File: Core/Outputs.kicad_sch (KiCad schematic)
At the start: 65 parts, among them J3 Conn_01x10_Female, J7 Conn_01x10_Female, Q14 2N7002, U10 TL072, U11 TL072, U12 TL072, U15 MAX5134, U2 TMUX1309, U4 TL072, U5 TL072, U6 TL072, U7 TL072, U8 TMUX1309, U9 TL072

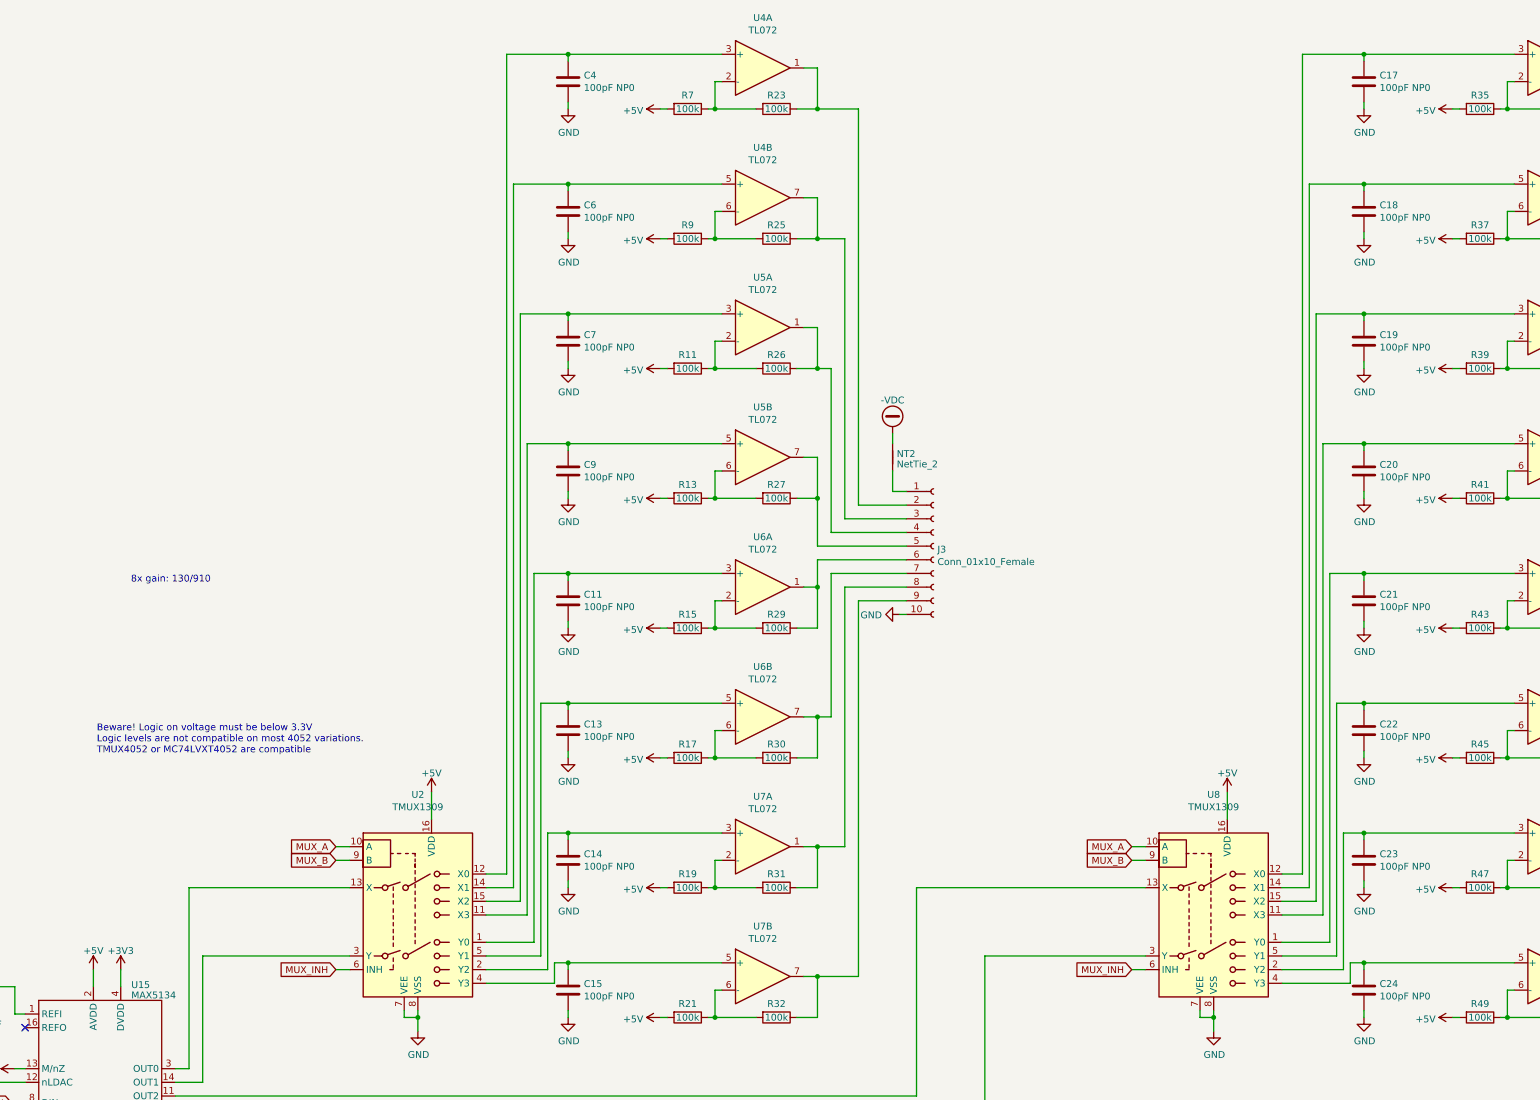
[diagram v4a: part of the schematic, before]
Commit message: Increase SnH capacitance
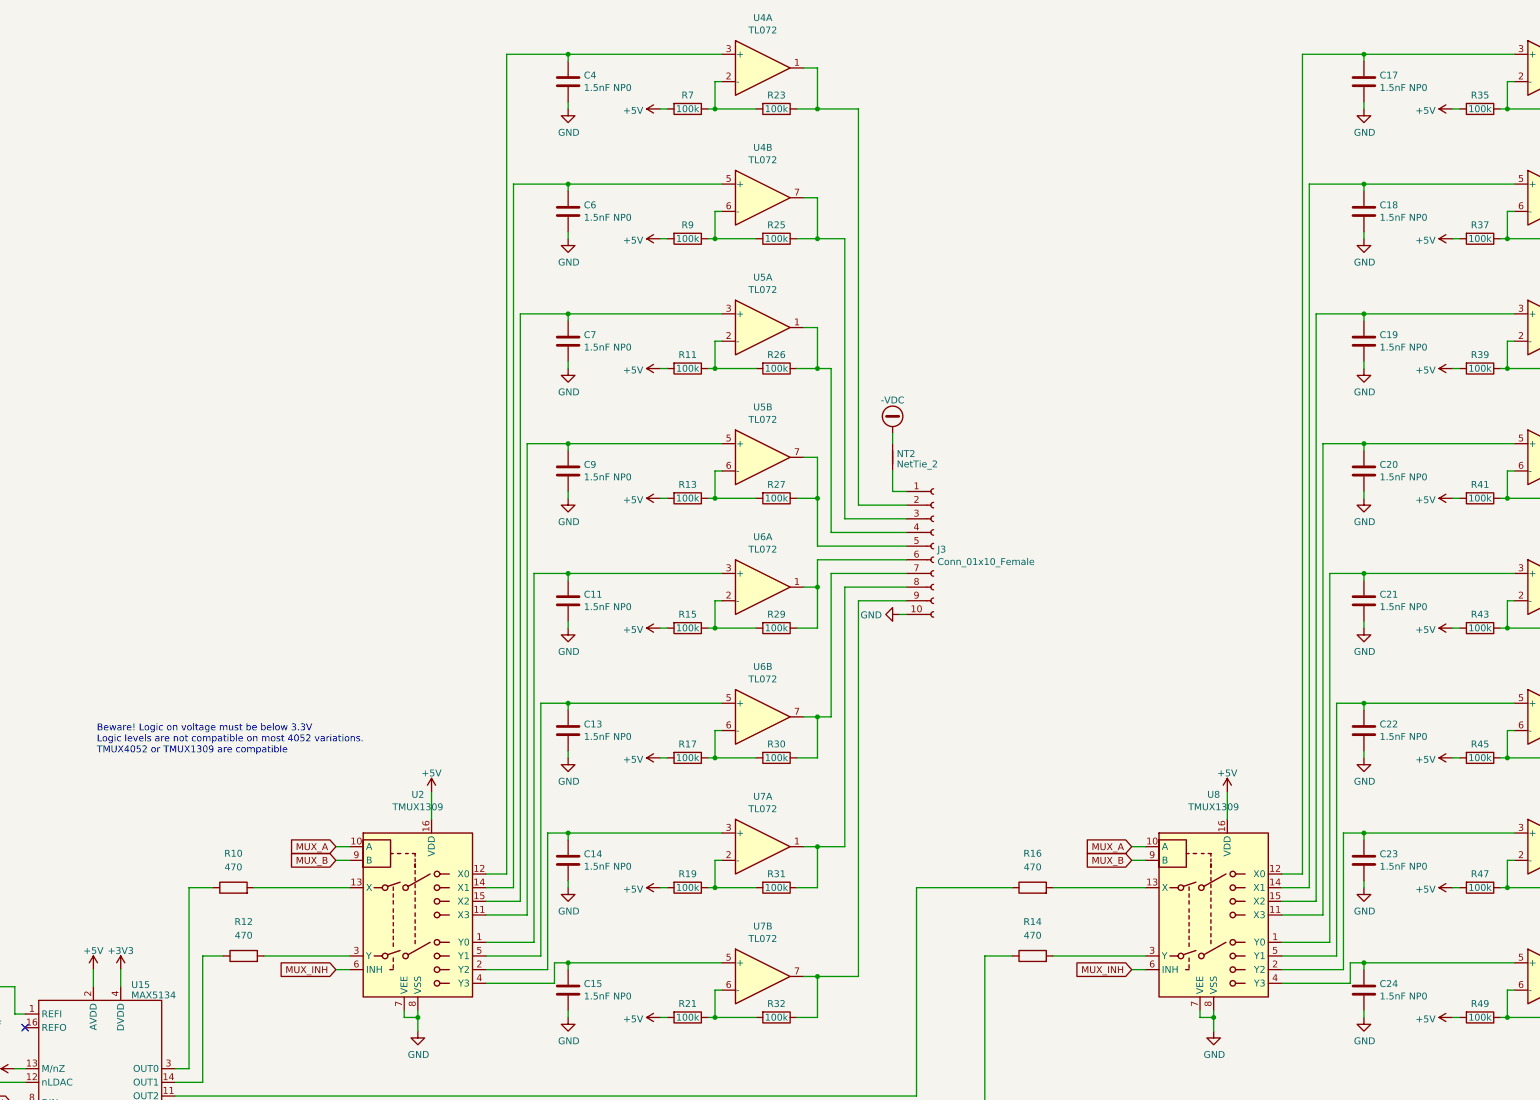
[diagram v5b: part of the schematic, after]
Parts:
- added R10, R12, R14, R16: 470, Resistor_SMD:R_0603_1608Metric, symbol Device:R
- C11, C13, C14, C15, C17, C18, C19, C20, C21, C22, C23, C24, C4, C6, C7, C9: value 100pF NP0 -> 1.5nF NP0
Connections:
- net at U15.11 (OUT2): now also R16.1; no longer U8.13 (X)
- net at U15.14 (OUT1): now also R12.1; no longer U2.3 (Y)
- net at U15.3 (OUT0): now also R10.1; no longer U2.13 (X)
- net at U15.6 (OUT3): now also R14.1; no longer U8.3 (Y)
- new net: R16.2, U8.13 (X)
- new net: R14.2, U8.3 (Y)
- new net: R10.2, U2.13 (X)
- new net: R12.2, U2.3 (Y)
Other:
- note added: "Beware! Logic on voltage must be below 3.3V Logic levels are not compatible on most 4052 variations. TMUX4052 or TMUX1309 are compatible"
- note removed: "8x gain: 130/910"
- note removed: "Beware! Logic on voltage must be below 3.3V Logic levels are not compatible on most 4052 variations. TMUX4052 or MC74LVXT4052 are compatible"
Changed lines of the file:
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@@
     (stroke (width 0) (type default))
   )
-  (wire (pts (xy 98.425 181.61) (xy 128.27 181.61))
+  (wire (pts (xy 98.425 181.61) (xy 102.87 181.61))
     (stroke (width 0) (type default))
   )
@@
     (stroke (width 0) (type default))
   )
+  (wire (pts (xy 112.395 194.31) (xy 128.27 194.31))
+    (stroke (width 0) (type default))
+  )
   (wire (pts (xy 316.865 85.09) (xy 316.865 83.82))
     (stroke (width 0) (type default))
@@
     (stroke (width 0) (type default))
   )
+  (wire (pts (xy 110.49 181.61) (xy 128.27 181.61))
+    (stroke (width 0) (type default))
+  )
   (wire (pts (xy 162.56 123.19) (xy 168.91 123.19))
     (stroke (width 0) (type default))
@@
     (stroke (width 0) (type default))
   )
-  (wire (pts (xy 246.38 194.31) (xy 276.225 194.31))
+  (wire (pts (xy 246.38 194.31) (xy 251.46 194.31))
     (stroke (width 0) (type default))
   )
@@
     (stroke (width 0) (type default))
   )
+  (wire (pts (xy 259.08 194.31) (xy 276.225 194.31))
+    (stroke (width 0) (type default))
+  )
   (wire (pts (xy 344.805 176.53) (xy 343.535 176.53))
     (stroke (width 0) (type default))
@@
     (stroke (width 0) (type default))
   )
-  (wire (pts (xy 100.965 194.31) (xy 128.27 194.31))
+  (wire (pts (xy 100.965 194.31) (xy 104.775 194.31))
     (stroke (width 0) (type default))
   )
@@
     (stroke (width 0) (type default))
   )
-  (wire (pts (xy 233.68 181.61) (xy 276.225 181.61))
+  (wire (pts (xy 233.68 181.61) (xy 251.46 181.61))
     (stroke (width 0) (type default))
   )
@@
     (stroke (width 0) (type default))
   )
+  (wire (pts (xy 259.08 181.61) (xy 276.225 181.61))
+    (stroke (width 0) (type default))
+  )
   (wire (pts (xy 196.215 205.74) (xy 203.835 205.74))
     (stroke (width 0) (type default))
@@
     (stroke (width 0) (type default))
   )
-  (text "8x gain: 130/910" (at 87.63 125.095 0)
-    (effects (font (size 1.27 1.27)) (justify left bottom))
-  )
-  (text "Beware! Logic on voltage must be below 3.3V\nLogic levels are not compatible on most 4052 variations.\nTMUX4052 or MC74LVXT4052 are compatible"
+  (text "Beware! Logic on voltage must be below 3.3V\nLogic levels are not compatible on most 4052 variations.\nTMUX4052 or TMUX1309 are compatible"
     (at 81.28 156.845 0)
     (effects (font (size 1.27 1.27)) (justify left bottom))
@@
       (effects (font (size 1.27 1.27)) (justify left))
     )
-    (property "Value" "100pF NP0" (at 171.831 201.803 0)
+    (property "Value" "1.5nF NP0" (at 171.831 201.803 0)
       (effects (font (size 1.27 1.27)) (justify left))
     )
@@
       (effects (font (size 1.27 1.27)) (justify left))
     )
-    (property "Value" "100pF NP0" (at 171.831 105.283 0)
+    (property "Value" "1.5nF NP0" (at 171.831 105.283 0)
       (effects (font (size 1.27 1.27)) (justify left))
     )
@@
       (effects (font (size 1.27 1.27)) (justify left))
     )
-    (property "Value" "100pF NP0" (at 319.786 153.543 0)
+    (property "Value" "1.5nF NP0" (at 319.786 153.543 0)
       (effects (font (size 1.27 1.27)) (justify left))
     )
@@
       (effects (font (size 1.27 1.27)) (justify left))
     )
-    (property "Value" "100pF NP0" (at 171.831 129.413 0)
+    (property "Value" "1.5nF NP0" (at 171.831 129.413 0)
       (effects (font (size 1.27 1.27)) (justify left))
     )
@@
       (effects (font (size 1.27 1.27)) (justify left))
     )
-    (property "Value" "100pF NP0" (at 171.831 153.543 0)
+    (property "Value" "1.5nF NP0" (at 171.831 153.543 0)
       (effects (font (size 1.27 1.27)) (justify left))
     )
@@
       (effects (font (size 1.27 1.27)) (justify left))
     )
-    (property "Value" "100pF NP0" (at 319.786 32.893 0)
+    (property "Value" "1.5nF NP0" (at 319.786 32.893 0)
       (effects (font (size 1.27 1.27)) (justify left))
     )
@@
     )
   )
+  (symbol (lib_id "Device:R") (at 106.68 181.61 90) (unit 1)
+    (in_bom yes) (on_board yes) (dnp no) (fields_autoplaced)
+    (property "Reference" "R10" (at 106.68 175.26 90)
+      (effects (font (size 1.27 1.27)))
+    )
+    (property "Value" "470" (at 106.68 177.8 90)
+      (effects (font (size 1.27 1.27)))
+    )
+    (property "Footprint" "Resistor_SMD:R_0603_1608Metric" (at 106.68 183.388 90)
+      (effects (font (size 1.27 1.27)) hide)
+    )
+    (property "Datasheet" "~" (at 106.68 181.61 0)
+      (effects (font (size 1.27 1.27)) hide)
+    )
+    (pin "1")
+    (pin "2")
+    (instances
+      (project "MIDI_CV16"
+        (path "/ba515087-2175-44fd-acc2-0e447df6195b/f58cfc93-0892-4036-8f05-b10b72ca44d6"
+          (reference "R10") (unit 1)
+        )
+      )
+    )
+  )
+  (symbol (lib_id "Device:R") (at 108.585 194.31 90) (unit 1)
+    (in_bom yes) (on_board yes) (dnp no) (fields_autoplaced)
+    (property "Reference" "R12" (at 108.585 187.96 90)
+      (effects (font (size 1.27 1.27)))
+    )
+    (property "Value" "470" (at 108.585 190.5 90)
+      (effects (font (size 1.27 1.27)))
+    )
+    (property "Footprint" "Resistor_SMD:R_0603_1608Metric" (at 108.585 196.088 90)
+      (effects (font (size 1.27 1.27)) hide)
+    )
+    (property "Datasheet" "~" (at 108.585 194.31 0)
+      (effects (font (size 1.27 1.27)) hide)
+    )
+    (pin "2")
+    (pin "1")
+    (instances
+      (project "MIDI_CV16"
+        (path "/ba515087-2175-44fd-acc2-0e447df6195b/f58cfc93-0892-4036-8f05-b10b72ca44d6"
+          (reference "R12") (unit 1)
+        )
+      )
+    )
+  )
   (symbol (lib_id "Device:R") (at 354.965 60.96 270) (unit 1)
     (in_bom yes) (on_board yes) (dnp no)
@@
       (effects (font (size 1.27 1.27)) (justify left))
     )
-    (property "Value" "100pF NP0" (at 171.831 32.893 0)
+    (property "Value" "1.5nF NP0" (at 171.831 32.893 0)
       (effects (font (size 1.27 1.27)) (justify left))
     )
@@
       (effects (font (size 1.27 1.27)) (justify left))
     )
-    (property "Value" "100pF NP0" (at 171.831 177.673 0)
+    (property "Value" "1.5nF NP0" (at 171.831 177.673 0)
       (effects (font (size 1.27 1.27)) (justify left))
     )
@@
       (effects (font (size 1.27 1.27)) (justify left))
     )
-    (property "Value" "100pF NP0" (at 171.831 81.153 0)
+    (property "Value" "1.5nF NP0" (at 171.831 81.153 0)
       (effects (font (size 1.27 1.27)) (justify left))
     )
@@
       (effects (font (size 1.27 1.27)) (justify left))
     )
-    (property "Value" "100pF NP0" (at 319.786 177.673 0)
+    (property "Value" "1.5nF NP0" (at 319.786 177.673 0)
       (effects (font (size 1.27 1.27)) (justify left))
     )
@@
       (effects (font (size 1.27 1.27)) (justify left))
     )
-    (property "Value" "100pF NP0" (at 319.786 201.803 0)
+    (property "Value" "1.5nF NP0" (at 319.786 201.803 0)
       (effects (font (size 1.27 1.27)) (justify left))
     )
@@
       (effects (font (size 1.27 1.27)) (justify left))
     )
-    (property "Value" "100pF NP0" (at 319.786 81.153 0)
+    (property "Value" "1.5nF NP0" (at 319.786 81.153 0)
       (effects (font (size 1.27 1.27)) (justify left))
     )
@@
       (effects (font (size 1.27 1.27)) (justify left))
     )
-    (property "Value" "100pF NP0" (at 319.786 105.283 0)
+    (property "Value" "1.5nF NP0" (at 319.786 105.283 0)
       (effects (font (size 1.27 1.27)) (justify left))
     )
@@
       (effects (font (size 1.27 1.27)) (justify left))
     )
-    (property "Value" "100pF NP0" (at 319.786 57.023 0)
+    (property "Value" "1.5nF NP0" (at 319.786 57.023 0)
       (effects (font (size 1.27 1.27)) (justify left))
     )
@@
     )
   )
+  (symbol (lib_id "Device:R") (at 255.27 194.31 90) (unit 1)
+    (in_bom yes) (on_board yes) (dnp no) (fields_autoplaced)
+    (property "Reference" "R14" (at 255.27 187.96 90)
+      (effects (font (size 1.27 1.27)))
+    )
+    (property "Value" "470" (at 255.27 190.5 90)
+      (effects (font (size 1.27 1.27)))
+    )
+    (property "Footprint" "Resistor_SMD:R_0603_1608Metric" (at 255.27 196.088 90)
+      (effects (font (size 1.27 1.27)) hide)
+    )
+    (property "Datasheet" "~" (at 255.27 194.31 0)
+      (effects (font (size 1.27 1.27)) hide)
+    )
+    (pin "2")
+    (pin "1")
+    (instances
+      (project "MIDI_CV16"
+        (path "/ba515087-2175-44fd-acc2-0e447df6195b/f58cfc93-0892-4036-8f05-b10b72ca44d6"
+          (reference "R14") (unit 1)
+        )
+      )
+    )
+  )
   (symbol (lib_id "Device:R") (at 191.135 109.22 270) (unit 1)
     (in_bom yes) (on_board yes) (dnp no)
@@
       (effects (font (size 1.27 1.27)) (justify left))
     )
-    (property "Value" "100pF NP0" (at 171.831 57.023 0)
+    (property "Value" "1.5nF NP0" (at 171.831 57.023 0)
       (effects (font (size 1.27 1.27)) (justify left))
     )
@@
     )
   )
+  (symbol (lib_id "Device:R") (at 255.27 181.61 90) (unit 1)
+    (in_bom yes) (on_board yes) (dnp no) (fields_autoplaced)
+    (property "Reference" "R16" (at 255.27 175.26 90)
+      (effects (font (size 1.27 1.27)))
+    )
+    (property "Value" "470" (at 255.27 177.8 90)
+      (effects (font (size 1.27 1.27)))
+    )
+    (property "Footprint" "Resistor_SMD:R_0603_1608Metric" (at 255.27 183.388 90)
+      (effects (font (size 1.27 1.27)) hide)
+    )
+    (property "Datasheet" "~" (at 255.27 181.61 0)
+      (effects (font (size 1.27 1.27)) hide)
+    )
+    (pin "2")
+    (pin "1")
+    (instances
+      (project "MIDI_CV16"
+        (path "/ba515087-2175-44fd-acc2-0e447df6195b/f58cfc93-0892-4036-8f05-b10b72ca44d6"
+          (reference "R16") (unit 1)
+        )
+      )
+    )
+  )
   (symbol (lib_id "Device:R") (at 207.645 60.96 270) (unit 1)
     (in_bom yes) (on_board yes) (dnp no)
@@
       (effects (font (size 1.27 1.27)) (justify left))
     )
-    (property "Value" "100pF NP0" (at 319.786 129.413 0)
+    (property "Value" "1.5nF NP0" (at 319.786 129.413 0)
       (effects (font (size 1.27 1.27)) (justify left))
     )
